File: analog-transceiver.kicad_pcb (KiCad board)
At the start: 2 copper layers, 99.1 x 73.7 mm, 172 parts, among them J2 AF In, J3 AF Out, Q1 2N3904, Q10 2N3904, Q11 2N3904, Q12 2N3904, Q13 2N3904, Q14 2N3904, Q15 2N3904, Q16 2N3904, Q17 2N3904, Q18 BF245A, Q19 2N3906, Q2 2N3904, Q20 2N3904, Q21 BF245A, Q22 2N3904, Q25 BD139, Q26 BD140, Q3 2N3904, SW1 SW_DPDT_x2, SW2 SW_DPDT_x2, T1 Transformer_1P_1S, Y1 10MHz, Y2 10MHz, Y3 10MHz, Y4 10MHz

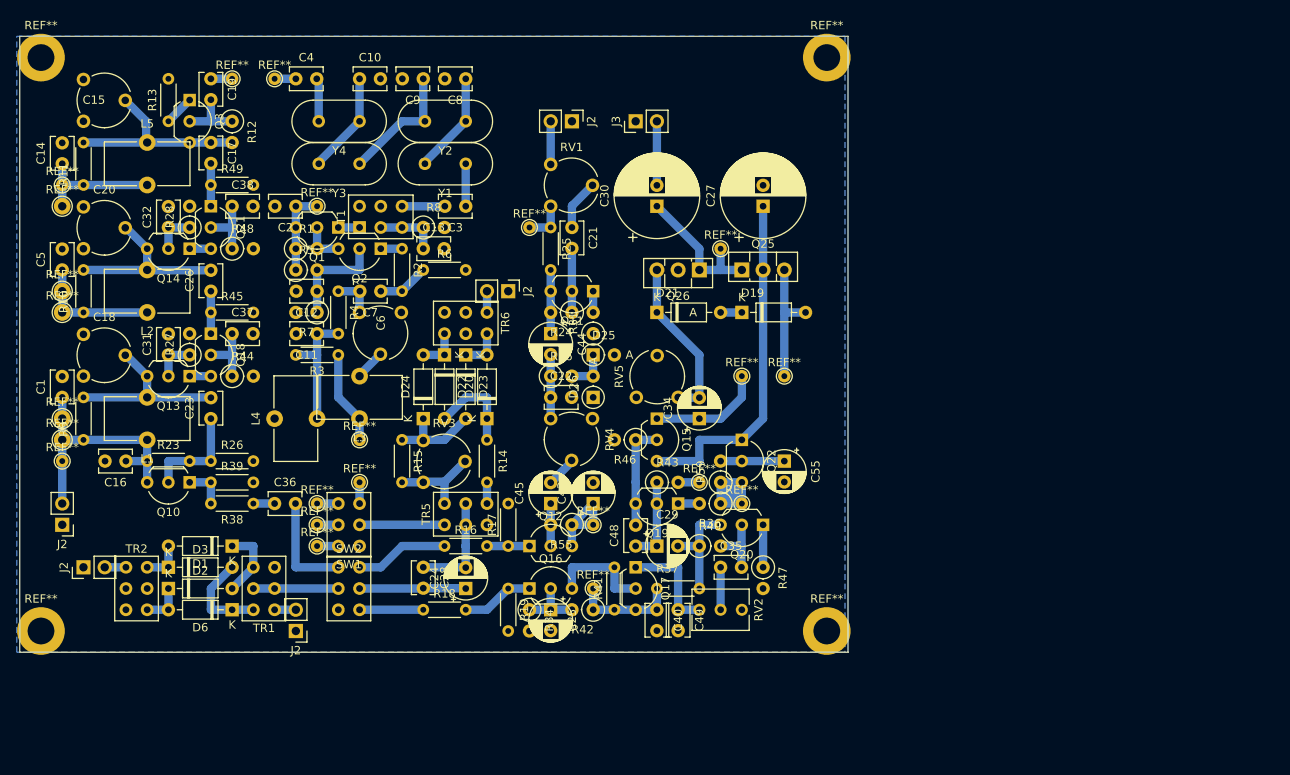
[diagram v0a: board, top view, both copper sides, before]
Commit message: New design + Rellay PTT + 1st Prototype v1.
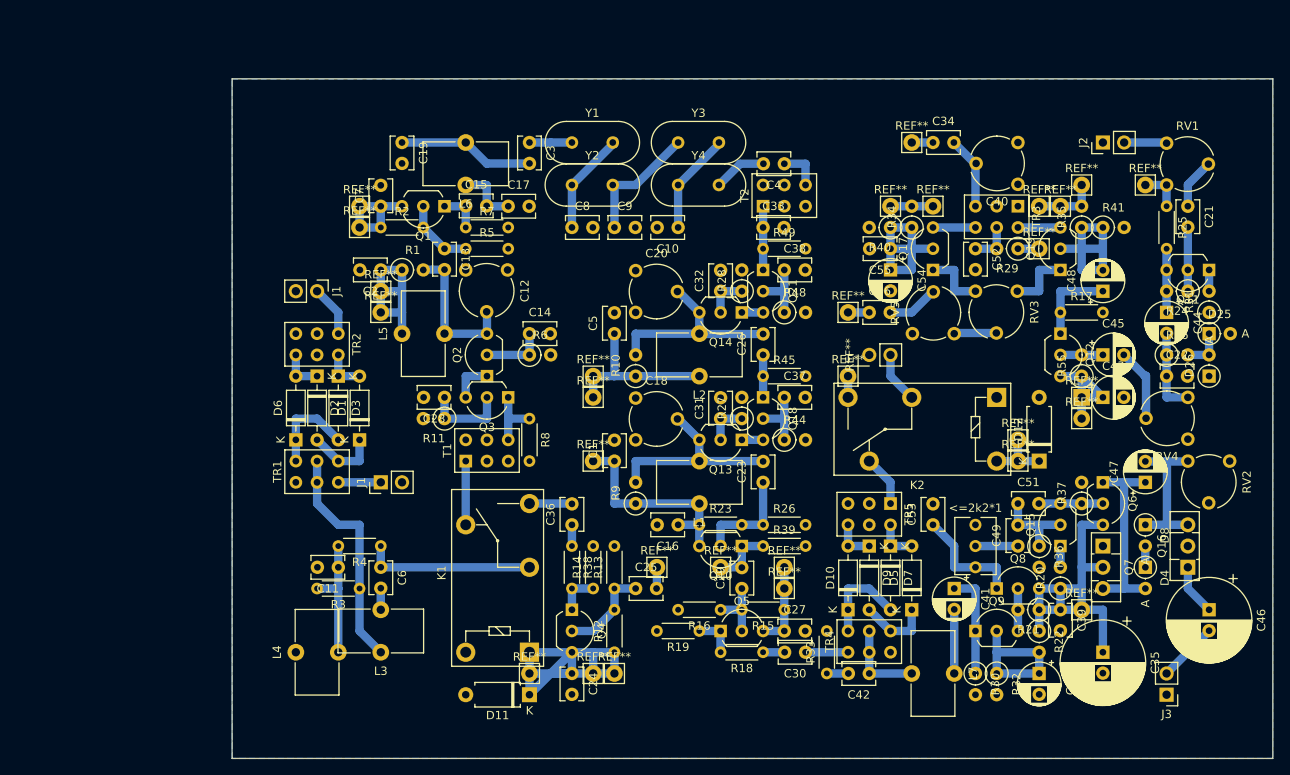
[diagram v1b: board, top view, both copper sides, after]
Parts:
- removed D19, D21: 1N4148, Diode_THT:D_DO-35_SOD27_P7.62mm_Horizontal
- removed D20, D22, D23, D24: BAT41, Diode_THT:D_DO-35_SOD27_P7.62mm_Horizontal
- removed the J2 at (106.7, 96.5)
- removed the J2 at (53.3, 124.5)
- removed the J2 at (55.9, 129.5)
- removed the J2 at (81.3, 137.2)
- removed the J2 at (114.3, 76.2)
- removed Q20, Q22: 2N3904, Package_TO_SOT_THT:TO-92_Inline_Wide
- removed Q25: BD139, Package_TO_SOT_THT:TO-126-3_Vertical
- removed Q26: BD140, Package_TO_SOT_THT:TO-126-3_Vertical
- removed R42: 82k, Resistor_THT:R_Axial_DIN0207_L6.3mm_D2.5mm_P2.54mm_Vertical
- removed R43: 330k, Resistor_THT:R_Axial_DIN0207_L6.3mm_D2.5mm_P2.54mm_Vertical
- removed R46: 2k2, Resistor_THT:R_Axial_DIN0207_L6.3mm_D2.5mm_P2.54mm_Vertical
- removed R47: 220, Resistor_THT:R_Axial_DIN0207_L6.3mm_D2.5mm_P2.54mm_Vertical
- removed R59: R, Resistor_THT:R_Axial_DIN0207_L6.3mm_D2.5mm_P2.54mm_Vertical
- removed the REF** at (83.8, 86.4)
- removed the REF** at (129.5, 119.4)
- removed the REF** at (139.7, 106.7)
- removed the REF** at (134.6, 106.7)
- removed the REF** at (53.3, 116.8)
- removed the REF** at (83.8, 127.0)
- removed the REF** at (83.8, 121.9)
- removed the REF** at (83.8, 124.5)
- removed the REF** at (88.9, 114.3)
- removed the REF** at (88.9, 119.4)
- removed the REF** at (53.3, 111.8)
- removed the REF** at (53.3, 83.8)
- removed the REF** at (53.3, 99.1)
- removed the REF** at (53.3, 114.3)
- removed the REF** at (53.3, 96.5)
- removed the REF** at (53.3, 86.4)
- removed the REF** at (144.8, 137.2)
- removed the REF** at (144.8, 68.6)
- removed the REF** at (50.8, 68.6)
- removed the REF** at (50.8, 137.2)
- removed the REF** at (78.7, 71.1)
- removed the REF** at (73.7, 71.1)
- removed the REF** at (109.2, 88.9)
- removed the REF** at (116.8, 124.5)
- removed the REF** at (134.6, 121.9)
- removed the REF** at (116.8, 132.1)
- removed the REF** at (132.1, 91.4)
- removed SW1, SW2: SW_DPDT_x2, Button_Switch_THT:SW_NKK_G1xJP
- removed TR6: 3x3 43-toroid, Button_Switch_THT:SW_NKK_G1xJP
- added <=2k2*1: 0, Potentiometer_THT:Potentiometer_Vishay_T73XW_Horizontal, F.Cu at (162.6, 124.5)
- added C33: ?, Capacitor_THT:C_Disc_D3.8mm_W2.6mm_P2.50mm, F.Cu at (137.2, 88.9)
- added C39: 100n, Capacitor_THT:C_Disc_D3.8mm_W2.6mm_P2.50mm, F.Cu at (172.7, 134.6)
- added C41: 10u, Capacitor_THT:CP_Radial_D5.0mm_P2.50mm, F.Cu at (160.0, 132.1)
- added C42: 330n, Capacitor_THT:C_Disc_D3.8mm_W2.6mm_P2.50mm, F.Cu at (149.9, 142.2)
- added C46: 220u, Capacitor_THT:CP_Radial_D10.0mm_P2.50mm, F.Cu at (190.5, 134.6)
- added C47: 1u, Capacitor_THT:CP_Radial_D5.0mm_P2.50mm, F.Cu at (182.9, 119.4)
- added C50: 100u, Capacitor_THT:CP_Radial_D5.0mm_P2.50mm, F.Cu at (170.2, 142.2)
- added C51: 820p needed?, Capacitor_THT:C_Disc_D3.8mm_W2.6mm_P2.50mm, F.Cu at (167.6, 121.9)
- added C52: C, Capacitor_THT:C_Disc_D3.8mm_W2.6mm_P2.50mm, F.Cu at (162.6, 91.4)
- added C53: 680n, Capacitor_THT:C_Disc_D3.8mm_W2.6mm_P2.50mm, F.Cu at (157.5, 124.5)
- added C54: CP, Capacitor_THT:CP_Radial_D5.0mm_P2.50mm, F.Cu at (152.4, 94.0)
- added C56: 100n, Capacitor_THT:C_Disc_D3.8mm_W2.6mm_P2.50mm, F.Cu at (149.9, 99.1)
- added D10: BAT41, Diode_THT:D_DO-35_SOD27_P7.62mm_Horizontal, F.Cu at (147.3, 134.6)
- added D11: 1n4007, Diode_THT:D_A-405_P7.62mm_Horizontal, F.Cu at (109.2, 144.8)
- added D12: 1n4007, Diode_THT:D_A-405_P7.62mm_Horizontal, F.Cu at (170.2, 116.8)
- added D4: 1N4148, Diode_THT:D_DO-35_SOD27_P2.54mm_Vertical_AnodeUp, F.Cu at (182.9, 129.5)
- added D5: BAT41, Diode_THT:D_DO-35_SOD27_P7.62mm_Horizontal, F.Cu at (154.9, 134.6)
- added D7: BAT41, Diode_THT:D_DO-35_SOD27_P7.62mm_Horizontal, F.Cu at (152.4, 127.0)
- added D8: 1N4148, Diode_THT:D_DO-35_SOD27_P2.54mm_Vertical_AnodeUp, F.Cu at (182.9, 124.5)
- added D9: BAT41, Diode_THT:D_DO-35_SOD27_P7.62mm_Horizontal, F.Cu at (149.9, 127.0)
- added J1: LO, Connector_PinHeader_2.54mm:PinHeader_1x02_P2.54mm_Vertical, F.Cu at (83.8, 96.5)
- added J1: BNC, Connector_PinHeader_2.54mm:PinHeader_1x02_P2.54mm_Vertical, F.Cu at (91.4, 119.4)
- added J2: AF In, Connector_PinHeader_2.54mm:PinHeader_1x02_P2.54mm_Vertical, F.Cu at (177.8, 78.7)
- added K1: G5Q-1, Relay_THT:Relay_SPDT_Omron-G5Q-1, F.Cu at (109.2, 139.7)
- added K2: G5Q-1, Relay_THT:Relay_SPDT_Omron-G5Q-1, F.Cu at (165.1, 109.2)
- added L6: 500n*, Inductor_THT:L_Toroid_Vertical_L10.0mm_W5.0mm_P5.08mm, F.Cu at (101.6, 83.8)
- added L7: 820u, Inductor_THT:L_Toroid_Vertical_L10.0mm_W5.0mm_P5.08mm, F.Cu at (160.0, 142.2)
- added Q4: 2N3904, Package_TO_SOT_THT:TO-92_Inline_Wide, F.Cu at (114.3, 134.6)
- added Q5: 2N3904, Package_TO_SOT_THT:TO-92_Inline_Wide, F.Cu at (132.1, 137.2)
- added Q6: 2N3904, Package_TO_SOT_THT:TO-92_Inline_Wide, F.Cu at (177.8, 119.4)
- added Q7: BD139, Package_TO_SOT_THT:TO-126-3_Vertical, F.Cu at (177.8, 127.0)
- added Q8: 2N3904, Package_TO_SOT_THT:TO-92_Inline_Wide, F.Cu at (165.1, 132.1)
- added Q9: 2N3904, Package_TO_SOT_THT:TO-92_Inline_Wide, F.Cu at (162.6, 137.2)
- added R20: 220, Resistor_THT:R_Axial_DIN0207_L6.3mm_D2.5mm_P2.54mm_Vertical, F.Cu at (172.7, 132.1)
- added R21: 10k, Resistor_THT:R_Axial_DIN0207_L6.3mm_D2.5mm_P2.54mm_Vertical, F.Cu at (170.2, 134.6)
- added R22: 15k, Resistor_THT:R_Axial_DIN0207_L6.3mm_D2.5mm_P2.54mm_Vertical, F.Cu at (170.2, 137.2)
- added R29: 470, Resistor_THT:R_Axial_DIN0207_L6.3mm_D2.5mm_P2.54mm_Vertical, F.Cu at (167.6, 91.4)
- added R30: 2k7, Resistor_THT:R_Axial_DIN0207_L6.3mm_D2.5mm_P2.54mm_Vertical, F.Cu at (162.6, 142.2)
- added R32: 3.3k, Resistor_THT:R_Axial_DIN0207_L6.3mm_D2.5mm_P2.54mm_Vertical, F.Cu at (165.1, 142.2)
- added R33: 50, Resistor_THT:R_Axial_DIN0204_L3.6mm_D1.6mm_P5.08mm_Horizontal, F.Cu at (144.8, 142.2)
- added R35: 4k7, Resistor_THT:R_Axial_DIN0207_L6.3mm_D2.5mm_P2.54mm_Vertical, F.Cu at (175.3, 88.9)
- added REF**: TestPoint_THTPad_2.0x2.0mm_Drill1.0mm, TestPoint:TestPoint_THTPad_2.0x2.0mm_Drill1.0mm, F.Cu at (91.4, 99.1)
- added REF**: TestPoint_THTPad_2.0x2.0mm_Drill1.0mm, TestPoint:TestPoint_THTPad_2.0x2.0mm_Drill1.0mm, F.Cu at (175.3, 111.8)
- added REF**: TestPoint_THTPad_2.0x2.0mm_Drill1.0mm, TestPoint:TestPoint_THTPad_2.0x2.0mm_Drill1.0mm, F.Cu at (116.8, 109.2)
- added REF**: PinHeader_1x02_P2.54mm_Vertical, Connector_PinHeader_2.54mm:PinHeader_1x02_P2.54mm_Vertical, F.Cu at (149.9, 104.1)
- added REF**: TestPoint_THTPad_2.0x2.0mm_Drill1.0mm, TestPoint:TestPoint_THTPad_2.0x2.0mm_Drill1.0mm, F.Cu at (152.4, 86.4)
- added REF**: TestPoint_THTPad_2.0x2.0mm_Drill1.0mm, TestPoint:TestPoint_THTPad_2.0x2.0mm_Drill1.0mm, F.Cu at (172.7, 86.4)
- added REF**: TestPoint_THTPad_2.0x2.0mm_Drill1.0mm, TestPoint:TestPoint_THTPad_2.0x2.0mm_Drill1.0mm, F.Cu at (157.5, 86.4)
- added REF**: TestPoint_THTPad_2.0x2.0mm_Drill1.0mm, TestPoint:TestPoint_THTPad_2.0x2.0mm_Drill1.0mm, F.Cu at (170.2, 86.4)
- added REF**: TestPoint_THTPad_2.0x2.0mm_Drill1.0mm, TestPoint:TestPoint_THTPad_2.0x2.0mm_Drill1.0mm, F.Cu at (170.2, 91.4)
- added REF**: TestPoint_THTPad_2.0x2.0mm_Drill1.0mm, TestPoint:TestPoint_THTPad_2.0x2.0mm_Drill1.0mm, F.Cu at (154.9, 78.7)
- added REF**: TestPoint_THTPad_2.0x2.0mm_Drill1.0mm, TestPoint:TestPoint_THTPad_2.0x2.0mm_Drill1.0mm, F.Cu at (175.3, 83.8)
- added REF**: TestPoint_THTPad_2.0x2.0mm_Drill1.0mm, TestPoint:TestPoint_THTPad_2.0x2.0mm_Drill1.0mm, F.Cu at (91.4, 96.5)
- added REF**: TestPoint_THTPad_2.0x2.0mm_Drill1.0mm, TestPoint:TestPoint_THTPad_2.0x2.0mm_Drill1.0mm, F.Cu at (182.9, 83.8)
- added REF**: TestPoint_THTPad_2.0x2.0mm_Drill1.0mm, TestPoint:TestPoint_THTPad_2.0x2.0mm_Drill1.0mm, F.Cu at (175.3, 109.2)
- added REF**: TestPoint_THTPad_2.0x2.0mm_Drill1.0mm, TestPoint:TestPoint_THTPad_2.0x2.0mm_Drill1.0mm, F.Cu at (116.8, 116.8)
- added REF**: TestPoint_THTPad_2.0x2.0mm_Drill1.0mm, TestPoint:TestPoint_THTPad_2.0x2.0mm_Drill1.0mm, F.Cu at (116.8, 106.7)
- added REF**: TestPoint_THTPad_2.0x2.0mm_Drill1.0mm, TestPoint:TestPoint_THTPad_2.0x2.0mm_Drill1.0mm, F.Cu at (132.1, 129.5)
- added REF**: TestPoint_THTPad_2.0x2.0mm_Drill1.0mm, TestPoint:TestPoint_THTPad_2.0x2.0mm_Drill1.0mm, F.Cu at (124.5, 129.5)
- added REF**: TestPoint_THTPad_2.0x2.0mm_Drill1.0mm, TestPoint:TestPoint_THTPad_2.0x2.0mm_Drill1.0mm, F.Cu at (109.2, 142.2)
- added REF**: TestPoint_THTPad_2.0x2.0mm_Drill1.0mm, TestPoint:TestPoint_THTPad_2.0x2.0mm_Drill1.0mm, F.Cu at (167.6, 116.8)
- added REF**: TestPoint_THTPad_2.0x2.0mm_Drill1.0mm, TestPoint:TestPoint_THTPad_2.0x2.0mm_Drill1.0mm, F.Cu at (175.3, 134.6)
- added REF**: TestPoint_THTPad_2.0x2.0mm_Drill1.0mm, TestPoint:TestPoint_THTPad_2.0x2.0mm_Drill1.0mm, F.Cu at (147.3, 99.1)
- added REF**: TestPoint_THTPad_2.0x2.0mm_Drill1.0mm, TestPoint:TestPoint_THTPad_2.0x2.0mm_Drill1.0mm, F.Cu at (88.9, 88.9)
- added REF**: TestPoint_THTPad_2.0x2.0mm_Drill1.0mm, TestPoint:TestPoint_THTPad_2.0x2.0mm_Drill1.0mm, F.Cu at (147.3, 106.7)
- added REF**: TestPoint_THTPad_2.0x2.0mm_Drill1.0mm, TestPoint:TestPoint_THTPad_2.0x2.0mm_Drill1.0mm, F.Cu at (88.9, 86.4)
- added REF**: TestPoint_THTPad_2.0x2.0mm_Drill1.0mm, TestPoint:TestPoint_THTPad_2.0x2.0mm_Drill1.0mm, F.Cu at (119.4, 142.2)
- added REF**: TestPoint_THTPad_2.0x2.0mm_Drill1.0mm, TestPoint:TestPoint_THTPad_2.0x2.0mm_Drill1.0mm, F.Cu at (139.7, 129.5)
- added REF**: TestPoint_THTPad_2.0x2.0mm_Drill1.0mm, TestPoint:TestPoint_THTPad_2.0x2.0mm_Drill1.0mm, F.Cu at (139.7, 132.1)
- added REF**: TestPoint_THTPad_2.0x2.0mm_Drill1.0mm, TestPoint:TestPoint_THTPad_2.0x2.0mm_Drill1.0mm, F.Cu at (116.8, 142.2)
- added REF**: TestPoint_THTPad_2.0x2.0mm_Drill1.0mm, TestPoint:TestPoint_THTPad_2.0x2.0mm_Drill1.0mm, F.Cu at (167.6, 114.3)
- added T2: iron powerder, Button_Switch_THT:SW_NKK_G1xJP, F.Cu at (137.2, 86.4)
- added TR3: 3x3 43-binocular, Button_Switch_THT:SW_NKK_G1xJP, F.Cu at (167.6, 86.4)
- added TR4: 3x3 43-toroid, Button_Switch_THT:SW_NKK_G1xJP, F.Cu at (147.3, 139.7)
- C11: value 0 -> 10n
- C12: value 100n -> 25p; footprint Capacitor_THT:C_Disc_D3.8mm_W2.6mm_P2.50mm -> Potentiometer_THT:Potentiometer_Piher_PT-6-V_Vertical
- C13: value 100n -> 5p6
- C15: value 25p -> 100n; footprint Potentiometer_THT:Potentiometer_Piher_PT-6-V_Vertical -> Capacitor_THT:C_Disc_D3.8mm_W2.6mm_P2.50mm
- C17: value 5p6 -> 2n*
- C19: value 100n -> 500p*
- C22: value 47n -> 47n*
- C24: value 10u -> 100n; footprint Capacitor_THT:CP_Radial_D5.0mm_P2.50mm -> Capacitor_THT:C_Disc_D3.8mm_W2.6mm_P2.50mm
- C25: value 4.7u -> 5p6; footprint Capacitor_THT:CP_Radial_D5.0mm_P2.50mm -> Capacitor_THT:C_Disc_D3.8mm_W2.6mm_P2.50mm
- C27: value 470u -> 100n; footprint Capacitor_THT:CP_Radial_D10.0mm_P2.50mm -> Capacitor_THT:C_Disc_D3.8mm_W2.6mm_P2.50mm
- C29: value 10u -> 5p6; footprint Capacitor_THT:CP_Radial_D5.0mm_P2.50mm -> Capacitor_THT:C_Disc_D3.8mm_W2.6mm_P2.50mm
- C30: value 220u -> 100n; footprint Capacitor_THT:CP_Radial_D10.0mm_P2.50mm -> Capacitor_THT:C_Disc_D3.8mm_W2.6mm_P2.50mm
- C34: value 1u -> 5p6; footprint Capacitor_THT:CP_Radial_D5.0mm_P2.50mm -> Capacitor_THT:C_Disc_D3.8mm_W2.6mm_P2.50mm
- C35: value 680n -> 470u; footprint Capacitor_THT:C_Disc_D3.8mm_W2.6mm_P2.50mm -> Capacitor_THT:CP_Radial_D10.0mm_P2.50mm
- C40: value 100n -> CTRIM; footprint Capacitor_THT:C_Disc_D3.8mm_W2.6mm_P2.50mm -> Potentiometer_THT:Potentiometer_Piher_PT-6-V_Vertical
- C48: value 820p -> CP; footprint Capacitor_THT:C_Disc_D3.8mm_W2.6mm_P2.50mm -> Capacitor_THT:CP_Radial_D5.0mm_P2.50mm
- C55: value CP -> C; footprint Capacitor_THT:CP_Radial_D5.0mm_P2.50mm -> Capacitor_THT:C_Disc_D3.8mm_W2.6mm_P2.50mm
- C6: value 0 -> 8.2p; footprint Potentiometer_THT:Potentiometer_Piher_PT-6-V_Vertical -> Capacitor_THT:C_Disc_D3.8mm_W2.6mm_P2.50mm
- L3: value 0 -> 26.981u
- L4: value 0 -> 22.124n
- Q15: value 2N3904 -> 2N3906
- Q16: value 2N3904 -> BD140; footprint Package_TO_SOT_THT:TO-92_Inline_Wide -> Package_TO_SOT_THT:TO-126-3_Vertical
- Q17: value 2N3904 -> 2n3904
- Q19: value 2N3906 -> 2n2904
- Q3: value 2N3904 -> BF245A
- R1: value R -> 6k8
- R10, R37, R9: footprint Resistor_THT:R_Axial_DIN0204_L3.6mm_D1.6mm_P5.08mm_Horizontal -> Resistor_THT:R_Axial_DIN0207_L6.3mm_D2.5mm_P2.54mm_Vertical
- R11: value 6k8 -> 330; footprint Resistor_THT:R_Axial_DIN0204_L3.6mm_D1.6mm_P5.08mm_Horizontal -> Resistor_THT:R_Axial_DIN0207_L6.3mm_D2.5mm_P2.54mm_Vertical
- R12: value 0 -> 180k; footprint Resistor_THT:R_Axial_DIN0207_L6.3mm_D2.5mm_P2.54mm_Vertical -> Resistor_THT:R_Axial_DIN0204_L3.6mm_D1.6mm_P5.08mm_Horizontal
- R13: value 0 -> N/A
- R14: value 10R -> 1k
- R15: value 15R -> 180k
- R16: value 47 -> N/A
- R17, R19: value 390? -> 1k
- R18: value 0 -> 39
- R2: value 0 -> 100K
- R23: value 100K -> 180k
- R34: value 56k -> 4k7
- R36: value 220 -> 330k
- R38: value 47 -> 39
- R39: value 390 -> 1k
- R40: value 330k -> 4k7
- R41: value 680 -> 4k7; footprint Resistor_THT:R_Axial_DIN0204_L3.6mm_D1.6mm_P5.08mm_Horizontal -> Resistor_THT:R_Axial_DIN0207_L6.3mm_D2.5mm_P2.54mm_Vertical
- R49: value 1M -> 1M*
- R5: value R -> N/A; footprint Resistor_THT:R_Axial_DIN0207_L6.3mm_D2.5mm_P2.54mm_Vertical -> Resistor_THT:R_Axial_DIN0204_L3.6mm_D1.6mm_P5.08mm_Horizontal
- R55: value 100k -> 180k
- R6: value R -> 10k; footprint Resistor_THT:R_Axial_DIN0204_L3.6mm_D1.6mm_P5.08mm_Horizontal -> Resistor_THT:R_Axial_DIN0207_L6.3mm_D2.5mm_P2.54mm_Vertical
- R7: value R -> 390; footprint Resistor_THT:R_Axial_DIN0207_L6.3mm_D2.5mm_P2.54mm_Vertical -> Resistor_THT:R_Axial_DIN0204_L3.6mm_D1.6mm_P5.08mm_Horizontal
- R8: value R -> 820; footprint Resistor_THT:R_Axial_DIN0207_L6.3mm_D2.5mm_P2.54mm_Vertical -> Resistor_THT:R_Axial_DIN0204_L3.6mm_D1.6mm_P5.08mm_Horizontal
- RV2: value 0 -> 5k; footprint Potentiometer_THT:Potentiometer_Vishay_T73XW_Horizontal -> Potentiometer_THT:Potentiometer_Piher_PT-6-V_Vertical
- RV3: value 100R -> 100
- RV5: value 5k -> 4k7
- T1: value Transformer_1P_1S -> 2:8 Turns 43-material? iron powder?
- moved J3 93.5 mm to (185.4, 144.8), turned to 180 degrees
- moved Q16 78.8 mm to (188.0, 129.5), turned to 90 degrees
- moved R12 78.2 mm to (119.4, 139.7), turned to 90 degrees
- moved R13 77.3 mm to (119.4, 132.1)
- moved RV4 76.2 mm to (188.0, 109.2), turned to 180 degrees
- moved R41 74.2 mm to (177.8, 88.9), turned to 0 degrees
- moved C21 73.7 mm to (188.0, 86.4)
- moved R24 73.7 mm to (188.0, 96.5)
- moved D25 73.7 mm to (190.5, 101.6)
- moved D26 73.7 mm to (190.5, 106.7)
- moved Q11 73.7 mm to (190.5, 94.0)
- moved R31 73.7 mm to (190.5, 99.1)
- moved C22 73.7 mm to (185.4, 106.7)
- moved C44 73.7 mm to (185.4, 99.1)
- moved R25 73.7 mm to (185.4, 86.4)
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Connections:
- C12 pad 1: Net-(C12-Pad1) -> GND
- C12 pad 2: GND -> Net-(C12-Pad2)
- C13 pad 2: GND -> Net-(C12-Pad2)
- C14 pad 1: +12V -> Net-(C14-Pad1)
- C15 pad 1: GND -> Net-(C15-Pad1)
- C17 pad 2: Net-(C17-Pad2) -> GND
- C19 pad 2: Net-(C19-Pad2) -> GND
- C2 pad 1: +12V -> +RX
- C24 pad 1: Net-(C24-Pad1) -> +TX
- C24 pad 2: Net-(C24-Pad2) -> GND
- C25 pad 2: GND -> Net-(C25-Pad2)
- C27 pad 1: Net-(C27-Pad1) -> +RX
- C28 pad 1: Net-(C24-Pad2) -> Net-(C28-Pad1)
- C28 pad 2: Net-(C24-Pad1) -> GND
- C29 pad 2: Net-(C29-Pad2) -> Net-(C25-Pad2)
- C3 pad 2: Net-(C3-Pad2) -> Net-(C19-Pad1)
- C34 pad 1: Net-(C34-Pad1) -> Net-(C13-Pad1)
- C35 pad 1: Net-(C35-Pad1) -> +RX
- C35 pad 2: Net-(C35-Pad2) -> GND
- C4 pad 1: Net-(C19-Pad1) -> Net-(C4-Pad1)
- C40 pad 1: +RX -> GND
- C40 pad 2: GND -> Net-(C34-Pad2)
- C48 pad 1: Net-(C29-Pad1) -> Net-(C48-Pad1)
- C49 pad 1: Net-(C49-Pad1) -> Net-(<=2k2*1-Pad2)
- C49 pad 2: GND -> Net-(C49-Pad2)
- C55 pad 1: Net-(C55-Pad1) -> Net-(C54-Pad1)
- C7 pad 1: Net-(C7-Pad1) -> +12V
- C7 pad 2: Net-(C6-Pad1) -> GND
- J3 pad 2: Net-(C30-Pad2) -> Net-(C46-Pad2)
- L5 pad 1: Net-(C15-Pad2) -> +RX
- L5 pad 2: +12V -> Net-(C12-Pad2)
- Q1 pad 1: Net-(Q1-Pad1) -> Net-(C15-Pad1)
- Q1 pad 2: Net-(Q1-Pad2) -> Net-(C13-Pad1)
- Q10 pad 1: Net-(Q10-Pad1) -> Net-(C25-Pad2)
- Q12 pad 1: Net-(Q12-Pad1) -> Net-(C48-Pad1)
- Q15 pad 1: Net-(C34-Pad1) -> Net-(Q15-Pad1)
- Q15 pad 2: Net-(C48-Pad2) -> Net-(C49-Pad2)
- Q15 pad 3: Net-(C27-Pad1) -> Net-(C51-Pad2)
- Q16 pad 1: Net-(Q16-Pad1) -> Net-(C46-Pad1)
- Q16 pad 2: Net-(C25-Pad1) -> GND
- Q16 pad 3: Net-(Q16-Pad3) -> Net-(C47-Pad2)
- Q17 pad 1: Net-(C49-Pad1) -> Net-(Q17-Pad1)
- Q17 pad 2: Net-(Q16-Pad3) -> Net-(C54-Pad1)
- Q17 pad 3: +RX -> Net-(Q17-Pad3)
- Q19 pad 2: Net-(C29-Pad1) -> Net-(C48-Pad2)
- Q19 pad 3: Net-(C48-Pad2) -> Net-(Q19-Pad3)
- Q2 pad 2: Net-(C12-Pad1) -> Net-(C14-Pad1)
- Q2 pad 3: Net-(Q1-Pad2) -> Net-(C12-Pad2)
- Q21 pad 1: Net-(C17-Pad2) -> Net-(C33-Pad1)
- Q3 pad 2: Net-(C19-Pad2) -> Net-(C28-Pad1)
- Q3 pad 3: Net-(C15-Pad2) -> Net-(Q2-Pad1)
- R1 pad 1: +12V -> +RX
- R1 pad 2: Net-(Q1-Pad2) -> Net-(C12-Pad2)
- R11 pad 1: +12V -> Net-(C28-Pad1)
- R11 pad 2: Net-(C15-Pad2) -> GND
- R12 pad 1: Net-(C19-Pad2) -> +TX
- R12 pad 2: Net-(C15-Pad2) -> Net-(C25-Pad1)
- R13 pad 1: Net-(Q3-Pad1) -> Net-(C25-Pad1)
- R14 pad 1: Net-(D20-Pad1) -> Net-(Q4-Pad1)
- R14 pad 2: Net-(R14-Pad2) -> GND
- R15 pad 1: Net-(D23-Pad2) -> +RX
- R15 pad 2: Net-(R15-Pad2) -> Net-(C29-Pad1)
- R16 pad 1: Net-(R16-Pad1) -> Net-(C29-Pad1)
- R16 pad 2: Net-(Q12-Pad1) -> GND
- R17 pad 1: Net-(Q12-Pad1) -> Net-(C48-Pad1)
- R18 pad 1: Net-(R18-Pad1) -> Net-(C30-Pad2)
- R18 pad 2: Net-(Q16-Pad1) -> Net-(Q5-Pad1)
- R19 pad 1: Net-(Q16-Pad1) -> Net-(Q5-Pad1)
- R2 pad 1: Net-(Q2-Pad1) -> +12V
- R2 pad 2: Net-(C7-Pad1) -> Net-(C13-Pad1)
- R34 pad 1: Net-(C25-Pad1) -> Net-(C54-Pad1)
- R34 pad 2: GND -> +TX
- R36 pad 1: +RX -> Net-(C49-Pad2)
- R36 pad 2: Net-(Q19-Pad1) -> Net-(C46-Pad1)
- R37 pad 1: +RX -> Net-(C51-Pad2)
- R37 pad 2: Net-(C29-Pad2) -> GND
- R38 pad 2: Net-(Q10-Pad1) -> Net-(Q4-Pad1)
- R39 pad 1: Net-(Q10-Pad1) -> Net-(C25-Pad2)
- R40 pad 1: Net-(C29-Pad2) -> Net-(C54-Pad1)
- R40 pad 2: Net-(C35-Pad2) -> GND
- R41 pad 1: +RX -> Net-(C48-Pad2)
- R41 pad 2: Net-(Q16-Pad3) -> GND
- R49 pad 1: Net-(C17-Pad2) -> Net-(C33-Pad1)
- R5 pad 1: +12V -> Net-(C13-Pad1)
- R5 pad 2: Net-(C12-Pad1) -> GND
- R6 pad 1: Net-(C7-Pad1) -> Net-(C14-Pad1)
- R6 pad 2: GND -> IFGain
- R7 pad 1: Net-(C12-Pad1) -> Net-(C15-Pad1)
- R8 pad 1: Net-(C13-Pad1) -> Net-(Q3-Pad1)
- RV2 pad 1: GND -> Net-(C47-Pad2)
- RV2 pad 2: Net-(C35-Pad1) -> GND
- RV2 pad 3: Net-(C49-Pad1) -> GND
- RV3 pad 1: Net-(R15-Pad2) -> Net-(Q17-Pad1)
- RV3 pad 2: Net-(R15-Pad2) -> Net-(RV3-Pad2)
- RV3 pad 3: Net-(D23-Pad2) -> Net-(Q19-Pad1)
- RV5 pad 1: Net-(C34-Pad2) -> Net-(RV3-Pad2)
- RV5 pad 2: GND -> Net-(C56-Pad2)
- T1 pad 1: Net-(Q1-Pad1) -> Net-(K1-Pad4)
- T1 pad 2: Net-(C13-Pad1) -> GND
- T1 pad 3: Net-(C13-Pad1) -> GND
- T1 pad 4: Net-(C3-Pad2) -> Net-(Q3-Pad1)
- T1 pad 5: GND -> (no net)
- T1 pad 6: GND -> (no net)
- TR1 pad 1: Net-(J1-Pad1) -> GND
- TR1 pad 2: Net-(SW1-Pad2) -> Net-(L3-Pad1)
- TR1 pad 3: GND -> Net-(J1-Pad1)
- TR1 pad 5: Net-(SW1-Pad2) -> Net-(L3-Pad1)
- TR5 pad 2: Net-(C24-Pad2) -> (no net)
- TR5 pad 4: Net-(R14-Pad2) -> Net-(D10-Pad2)
- TR5 pad 5: Net-(C24-Pad2) -> GND
- TR5 pad 6: Net-(R15-Pad2) -> Net-(D5-Pad2)
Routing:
- net +TX: track 18.8 -> 84.4 mm
- net Net-(C27-Pad1): track 41.7 -> 0.00 mm
- net +RX: track 32.6 -> 71.1 mm
- net Net-(C34-Pad1): track 29.0 -> 0.00 mm
- net Net-(C47-Pad1): track 0.00 -> 22.9 mm
- net Net-(C54-Pad1): track 0.00 -> 20.3 mm
- net Net-(C12-Pad2): track 0.00 -> 17.9 mm
- net Net-(C50-Pad1): track 0.00 -> 17.8 mm
- net Net-(C47-Pad2): track 0.00 -> 17.8 mm
- net Net-(C15-Pad2): track 23.9 -> 7.63 mm
- net +12V: track 73.7 -> 58.4 mm
- net Net-(C6-Pad1): track 5.14 -> 20.3 mm
- net Net-(C30-Pad1): track 19.9 -> 5.08 mm
- net Net-(<=2k2*1-Pad3): track 0.00 -> 13.8 mm
- net Net-(L3-Pad1): track 13.8 -> 27.5 mm
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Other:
- board size 99.1 x 73.7 mm -> 124.5 x 81.3 mm
